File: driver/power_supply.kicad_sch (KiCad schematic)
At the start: 15 parts, among them J2 PJ-051AH, U2 LT323AT#PBF, U6 MCP1700-3302E/TO, U7 MCP1700-3002E/TO

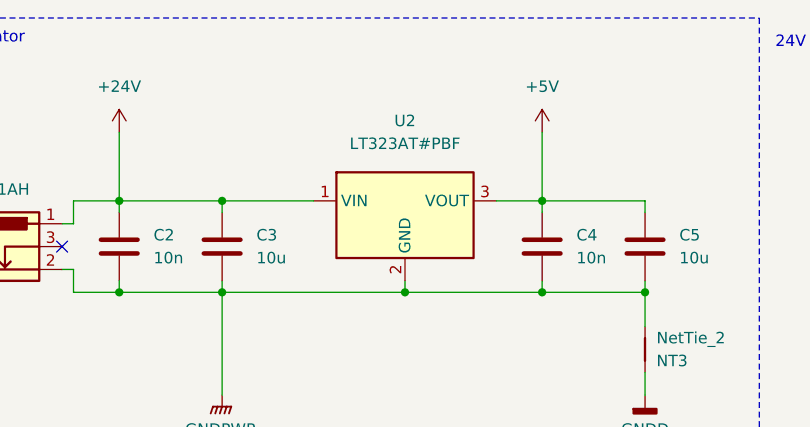
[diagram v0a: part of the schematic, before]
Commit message: Replaced 5V regulator with fully compatible alternative
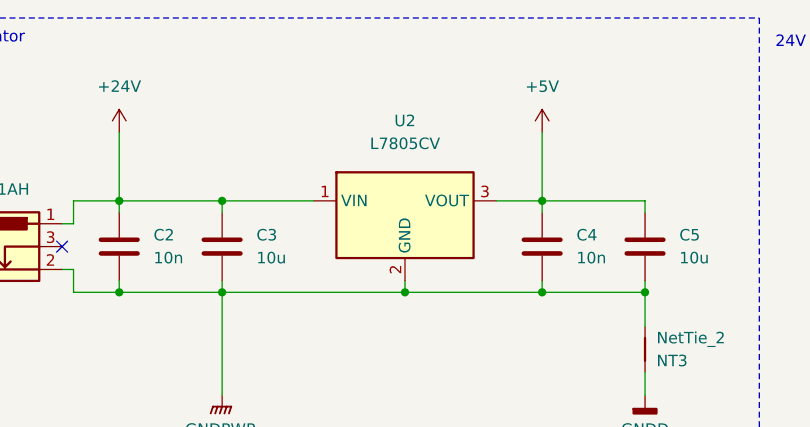
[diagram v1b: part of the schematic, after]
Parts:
- U2: value LT323AT#PBF -> L7805CV; symbol Custom_Regulator_Linear:LM323 -> Custom_Regulator_Linear:L78xx
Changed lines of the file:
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@@
 		(title "Reflow Soldering Hot Plate Driver")
 		(date "2024-07-30")
-		(rev "v1.0.0")
+		(rev "v1.1.0")
 	)
 	(junction
@@
 	)
 	(symbol
-		(lib_id "Custom_Regulator_Linear:LM323")
+		(lib_id "Custom_Regulator_Linear:L78xx")
 		(at 68.58 36.83 0)
 		(unit 1)
@@
 			)
 		)
-		(property "Value" "LT323AT#PBF"
+		(property "Value" "L7805CV"
 			(at 68.58 27.94 0)
 			(effects
@@
 		)
 		(property "Footprint" "Package_TO_SOT_THT:TO-220-3_Horizontal_TabDown"
-			(at 68.58 29.21 0)
-			(effects
-				(font
-					(size 1.27 1.27)
-				)
-				(hide yes)
-			)
+			(at 66.04 29.21 0)
+			(effects
+				(font
+					(size 1.27 1.27)
+				)
+				(justify left)
+				(hide yes)
+			)
